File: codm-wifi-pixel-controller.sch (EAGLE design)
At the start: 45 parts, among them U1 AP62XXX-TSOT26, U2 REG710NA-5/250, U3 SN74AHCT125D, U4 ESP-WROOM-32

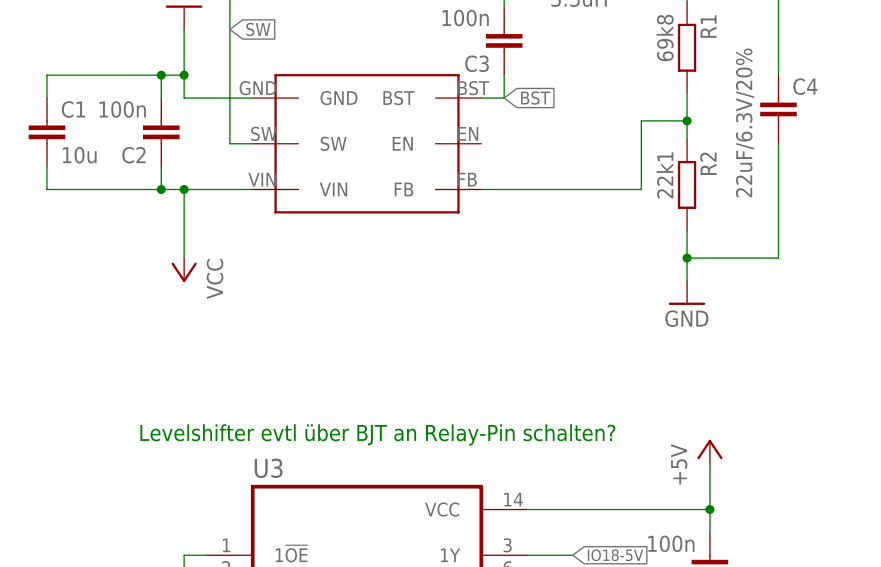
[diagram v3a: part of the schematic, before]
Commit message: added reverse polarity protection
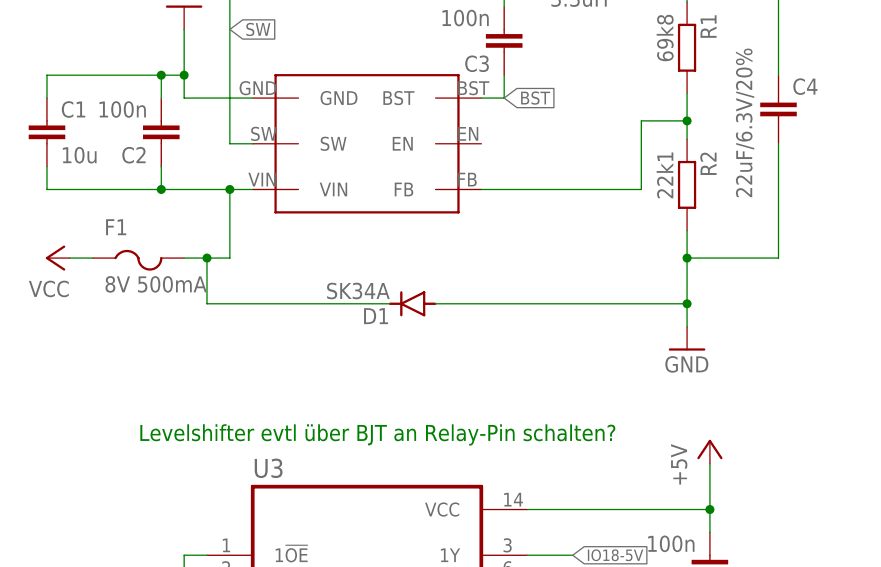
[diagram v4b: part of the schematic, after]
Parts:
- added D1: SK34A, diode:DIODE-DO214AC
- added F1: 8V 500mA, adafruit:PTCFUSE-1206
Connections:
- new net VCCF: C1.2, C2.1, D1.C, F1.2, U1.VIN
- net GND: now also D1.A
- net VCC: now also F1.1; no longer C1.2, C2.1, U1.VIN
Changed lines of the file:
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@@
 <part name="TP14" library="testpad" library_urn="urn:adsk.eagle:library:385" deviceset="PTR1" device="TP14R" package3d_urn="urn:adsk.eagle:package:27966/1" override_package3d_urn="urn:adsk.eagle:package:33701212/2" override_package_urn="urn:adsk.eagle:footprint:27923/1" value="PTR1TP14R"/>
 <part name="TP15" library="testpad" library_urn="urn:adsk.eagle:library:385" deviceset="PTR1" device="TP14R" package3d_urn="urn:adsk.eagle:package:27966/1" value="PTR1TP14R"/>
+<part name="D1" library="diode" deviceset="DIODE-" device="DO214AC" package3d_urn="urn:adsk.eagle:package:43417/2" value="SK34A"/>
+<part name="F1" library="adafruit" library_urn="urn:adsk.eagle:library:420" deviceset="PTCFUSE" device="-1206" package3d_urn="urn:adsk.eagle:package:6240569/1" override_package3d_urn="urn:adsk.eagle:package:20945049/2" override_package_urn="urn:adsk.eagle:footprint:6239923/1" value="8V 500mA"/>
 </parts>
 <sheets>
@@
 </instance>
 <instance part="U1" gate="G$1" x="45.72" y="139.7" smashed="yes"/>
-<instance part="P+3" gate="VCC" x="25.4" y="124.46" smashed="yes" rot="R180">
-<attribute name="VALUE" x="27.94" y="127" size="1.778" layer="96" rot="R270"/>
+<instance part="P+3" gate="VCC" x="10.16" y="127" smashed="yes" rot="R90">
+<attribute name="VALUE" x="12.7" y="124.46" size="1.778" layer="96" rot="R180"/>
 </instance>
 <instance part="GND5" gate="1" x="25.4" y="154.94" smashed="yes" rot="R180">
@@
 <attribute name="VALUE" x="77.978" y="138.938" size="1.778" layer="96" rot="R270"/>
 </instance>
-<instance part="GND3" gate="1" x="81.28" y="121.92" smashed="yes">
-<attribute name="VALUE" x="78.74" y="119.38" size="1.778" layer="96"/>
+<instance part="GND3" gate="1" x="81.28" y="116.84" smashed="yes">
+<attribute name="VALUE" x="78.74" y="114.3" size="1.778" layer="96"/>
 </instance>
 <instance part="C4" gate="G$1" x="91.44" y="144.78" smashed="yes">
@@
 <attribute name="NAME" x="92.964" y="41.91" size="1.778" layer="95" rot="R90"/>
 <attribute name="TP_SIGNAL_NAME" x="95.25" y="45.72" size="1.778" layer="97"/>
+</instance>
+<instance part="D1" gate="G$1" x="50.8" y="121.92" smashed="yes" rot="R180">
+<attribute name="NAME" x="48.26" y="121.4374" size="1.778" layer="95" rot="R180"/>
+<attribute name="VALUE" x="48.26" y="124.2314" size="1.778" layer="96" rot="R180"/>
+</instance>
+<instance part="F1" gate="G$1" x="20.32" y="124.46" smashed="yes">
+<attribute name="VALUE" x="16.51" y="123.19" size="1.778" layer="96"/>
+<attribute name="NAME" x="16.51" y="129.54" size="1.778" layer="95"/>
 </instance>
 </instances>
@@
 <pinref part="GND3" gate="1" pin="GND"/>
 <pinref part="C4" gate="G$1" pin="2"/>
-<wire x1="81.28" y1="127" x2="81.28" y2="124.46" width="0.1524" layer="91"/>
+<wire x1="81.28" y1="127" x2="81.28" y2="121.92" width="0.1524" layer="91"/>
+<wire x1="81.28" y1="121.92" x2="81.28" y2="119.38" width="0.1524" layer="91"/>
 <wire x1="91.44" y1="139.7" x2="91.44" y2="127" width="0.1524" layer="91"/>
 <wire x1="81.28" y1="127" x2="91.44" y2="127" width="0.1524" layer="91"/>
 <junction x="81.28" y="127"/>
+<pinref part="D1" gate="G$1" pin="A"/>
+<wire x1="81.28" y1="121.92" x2="53.34" y2="121.92" width="0.1524" layer="91"/>
+<junction x="81.28" y="121.92"/>
 </segment>
 <segment>
@@
 </segment>
 <segment>
+<pinref part="F1" gate="G$1" pin="1"/>
+<wire x1="15.24" y1="127" x2="12.7" y2="127" width="0.1524" layer="91"/>
 <pinref part="P+3" gate="VCC" pin="VCC"/>
-<wire x1="25.4" y1="127" x2="25.4" y2="134.62" width="0.1524" layer="91"/>
-<pinref part="U1" gate="G$1" pin="VIN"/>
-<wire x1="25.4" y1="134.62" x2="33.02" y2="134.62" width="0.1524" layer="91"/>
-<wire x1="25.4" y1="134.62" x2="22.86" y2="134.62" width="0.1524" layer="91"/>
-<junction x="25.4" y="134.62"/>
-<pinref part="C1" gate="G$1" pin="2"/>
-<wire x1="22.86" y1="134.62" x2="10.16" y2="134.62" width="0.1524" layer="91"/>
-<wire x1="10.16" y1="134.62" x2="10.16" y2="137.16" width="0.1524" layer="91"/>
-<pinref part="C2" gate="G$1" pin="1"/>
-<wire x1="22.86" y1="137.16" x2="22.86" y2="134.62" width="0.1524" layer="91"/>
-<junction x="22.86" y="134.62"/>
 </segment>
 </net>
@@
 </segment>
 </net>
+<net name="VCCF" class="0">
+<segment>
+<pinref part="D1" gate="G$1" pin="C"/>
+<wire x1="27.94" y1="127" x2="30.48" y2="127" width="0.1524" layer="91"/>
+<wire x1="48.26" y1="121.92" x2="27.94" y2="121.92" width="0.1524" layer="91"/>
+<wire x1="27.94" y1="121.92" x2="27.94" y2="127" width="0.1524" layer="91"/>
+<junction x="27.94" y="127"/>
+<pinref part="F1" gate="G$1" pin="2"/>
+<wire x1="25.4" y1="127" x2="27.94" y2="127" width="0.1524" layer="91"/>
+<wire x1="22.86" y1="134.62" x2="30.48" y2="134.62" width="0.1524" layer="91"/>
+<pinref part="C1" gate="G$1" pin="2"/>
+<wire x1="22.86" y1="134.62" x2="10.16" y2="134.62" width="0.1524" layer="91"/>
+<wire x1="10.16" y1="134.62" x2="10.16" y2="137.16" width="0.1524" layer="91"/>
+<pinref part="C2" gate="G$1" pin="1"/>
+<wire x1="22.86" y1="137.16" x2="22.86" y2="134.62" width="0.1524" layer="91"/>
+<junction x="22.86" y="134.62"/>
+<wire x1="30.48" y1="127" x2="30.48" y2="134.62" width="0.1524" layer="91"/>
+<pinref part="U1" gate="G$1" pin="VIN"/>
+<wire x1="33.02" y1="134.62" x2="30.48" y2="134.62" width="0.1524" layer="91"/>
+<junction x="30.48" y="134.62"/>
+</segment>
+</net>

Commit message: new version 0.7.4 with fixes
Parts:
- removed C8: 100n, rcl:C-EUC0603K
- added TP16: PTR1TP14R, testpad:PTR1TP14R
- JP1: device pinhead:PINHD-1X5 -> codm:PINHD-1X5
- U3: value SN74AHCT125D -> SN74AHCT125PWR; device SN74AHCT125D:SN74AHCT125D -> SN74AHCT125PWR:SN74AHCT125PWR
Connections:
- net BTN: now also S1.1; no longer S1.2
- net GND: now also FLASH.4, RESET.3, S1.2, TP16.TP, U3.!1OE, U3.!2OE, U3.!3OE, U3.!4OE; no longer C8.1, FLASH.2, RESET.1, S1.1, U3.1!OE, U3.2!OE, U3.3!OE, U3.4!OE
- net RESET: no longer C8.2
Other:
- note added: "WLAN Pixel Controller V0.7.4 codm.de, 2022 CC-BY-NC-SA"
- note removed: "WLAN Pixel Controller V0.7 codm.de, 2022 CC-BY-NC-SA"

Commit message: finetuning 0.7.4
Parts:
- removed R5: 10k, rcl:R-EU_R0603
- F1: value 8V 500mA -> 24V 500mA
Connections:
- net +3V3: no longer R5.1
- net GPIO0: no longer R5.2
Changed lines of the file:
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@@
 <part name="R4" library="rcl" deviceset="R-EU_" device="R0603" package3d_urn="urn:adsk.eagle:package:23555/3" value="10k"/>
 <part name="C5" library="rcl" deviceset="C-EU" device="C0603K" package3d_urn="urn:adsk.eagle:package:23680/2" value="1u"/>
-<part name="R5" library="rcl" deviceset="R-EU_" device="R0603" package3d_urn="urn:adsk.eagle:package:23555/3" value="10k"/>
-<part name="+3V3" library="supply1" deviceset="+3V3" device=""/>
 <part name="GND4" library="supply1" deviceset="GND" device=""/>
 <part name="U1" library="codm" library_urn="urn:adsk.eagle:library:11602856" deviceset="AP62XXX-TSOT26" device="" package3d_urn="urn:adsk.eagle:package:33659716/2"/>
@@
 <part name="TP15" library="testpad" library_urn="urn:adsk.eagle:library:385" deviceset="PTR1" device="TP14R" package3d_urn="urn:adsk.eagle:package:27966/1" value="PTR1TP14R"/>
 <part name="D1" library="diode" deviceset="DIODE-" device="DO214AC" package3d_urn="urn:adsk.eagle:package:43417/2" value="SK34A"/>
-<part name="F1" library="adafruit" library_urn="urn:adsk.eagle:library:420" deviceset="PTCFUSE" device="-1206" package3d_urn="urn:adsk.eagle:package:6240569/1" override_package3d_urn="urn:adsk.eagle:package:20945049/2" override_package_urn="urn:adsk.eagle:footprint:6239923/1" value="8V 500mA"/>
+<part name="F1" library="adafruit" library_urn="urn:adsk.eagle:library:420" deviceset="PTCFUSE" device="-1206" package3d_urn="urn:adsk.eagle:package:6240569/1" override_package3d_urn="urn:adsk.eagle:package:20945049/2" override_package_urn="urn:adsk.eagle:footprint:6239923/1" value="24V 500mA"/>
 <part name="TP16" library="testpad" library_urn="urn:adsk.eagle:library:385" deviceset="PTR1" device="TP14R" package3d_urn="urn:adsk.eagle:package:27966/1" value="PTR1TP14R"/>
 </parts>
@@
 <attribute name="NAME" x="153.416" y="83.439" size="1.778" layer="95" rot="R180"/>
 <attribute name="VALUE" x="153.416" y="88.519" size="1.778" layer="96" rot="R180"/>
-</instance>
-<instance part="R5" gate="G$1" x="231.14" y="89.408" smashed="yes" rot="R270">
-<attribute name="NAME" x="232.6386" y="93.218" size="1.778" layer="95" rot="R270"/>
-<attribute name="VALUE" x="227.838" y="93.218" size="1.778" layer="96" rot="R270"/>
-</instance>
-<instance part="+3V3" gate="G$1" x="231.14" y="111.76" smashed="yes">
-<attribute name="VALUE" x="228.6" y="106.68" size="1.778" layer="96" rot="R90"/>
 </instance>
 <instance part="GND4" gate="1" x="66.04" y="10.16" smashed="yes">
@@
 </segment>
 <segment>
-<pinref part="+3V3" gate="G$1" pin="+3V3"/>
-<pinref part="R5" gate="G$1" pin="1"/>
-<wire x1="231.14" y1="109.22" x2="231.14" y2="94.488" width="0.1524" layer="91"/>
-</segment>
-<segment>
 <pinref part="L1" gate="G$1" pin="2"/>
 <wire x1="78.74" y1="157.48" x2="81.28" y2="157.48" width="0.1524" layer="91"/>
@@
 <segment>
 <pinref part="U4" gate="G$1" pin="IO0"/>
-<wire x1="231.14" y1="50.8" x2="223.52" y2="50.8" width="0.1524" layer="91"/>
-<pinref part="R5" gate="G$1" pin="2"/>
-<wire x1="231.14" y1="84.328" x2="231.14" y2="50.8" width="0.1524" layer="91"/>
+<wire x1="233.68" y1="50.8" x2="223.52" y2="50.8" width="0.1524" layer="91"/>
 <pinref part="FLASH" gate="G$1" pin="1"/>
-<wire x1="231.14" y1="50.8" x2="233.68" y2="50.8" width="0.1524" layer="91"/>
-<junction x="231.14" y="50.8"/>
 </segment>
 </net>
@@
 <segment>
 <pinref part="D1" gate="G$1" pin="C"/>
-<wire x1="27.94" y1="127" x2="30.48" y2="127" width="0.1524" layer="91"/>
-<wire x1="48.26" y1="121.92" x2="27.94" y2="121.92" width="0.1524" layer="91"/>
-<wire x1="27.94" y1="121.92" x2="27.94" y2="127" width="0.1524" layer="91"/>
-<junction x="27.94" y="127"/>
+<wire x1="48.26" y1="121.92" x2="30.48" y2="121.92" width="0.1524" layer="91"/>
+<wire x1="30.48" y1="121.92" x2="30.48" y2="127" width="0.1524" layer="91"/>
+<junction x="30.48" y="127"/>
 <pinref part="F1" gate="G$1" pin="2"/>
-<wire x1="25.4" y1="127" x2="27.94" y2="127" width="0.1524" layer="91"/>
+<wire x1="25.4" y1="127" x2="30.48" y2="127" width="0.1524" layer="91"/>
 <wire x1="22.86" y1="134.62" x2="30.48" y2="134.62" width="0.1524" layer="91"/>
 <pinref part="C1" gate="G$1" pin="2"/>

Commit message: after prototype 0.7.4 - final 0.8
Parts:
- removed C12: 100n, rcl:C-EUC0603K
- added C8: 2.2uF, rcl:C-EUC0603K
- C11: value 2.2uF -> 100n
- renumbered R6 to R5
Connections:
- net +3V3: now also C9.2; no longer C10.2
- net +5V: now also C10.2; no longer C12.2
- net GND: now also C9.1; no longer C12.1
- net N$5: now also C8.1; no longer C9.1
- net N$8: now also C8.2; no longer C9.2
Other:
- moved on the sheet: C10, C11, C9
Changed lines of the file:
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@@
 <part name="U3" library="SN74AHCT125PWR" deviceset="SN74AHCT125PWR" device="" override_package3d_urn="urn:adsk.eagle:package:23111573/4" override_package_urn="urn:adsk.eagle:footprint:23111574/2" override_locally_modified="yes"/>
 <part name="GND2" library="supply1" deviceset="GND" device=""/>
-<part name="C12" library="rcl" deviceset="C-EU" device="C0603K" package3d_urn="urn:adsk.eagle:package:23680/2" value="100n"/>
+<part name="C11" library="rcl" deviceset="C-EU" device="C0603K" package3d_urn="urn:adsk.eagle:package:23680/2" value="100n"/>
 <part name="GND6" library="supply1" deviceset="GND" device=""/>
 <part name="P+2" library="supply1" library_urn="urn:adsk.eagle:library:371" deviceset="+5V" device=""/>
@@
 <part name="C2" library="rcl" deviceset="C-EU" device="C0603K" package3d_urn="urn:adsk.eagle:package:23680/2" value="100n"/>
 <part name="U2" library="REG710NA-5_250" deviceset="REG710NA-5/250" device="" override_package3d_urn="urn:adsk.eagle:package:30503030/3" override_package_urn="urn:adsk.eagle:footprint:30503033/1" override_locally_modified="yes"/>
+<part name="C9" library="rcl" deviceset="C-EU" device="C0603K" package3d_urn="urn:adsk.eagle:package:23680/2" value="2.2uF"/>
 <part name="C10" library="rcl" deviceset="C-EU" device="C0603K" package3d_urn="urn:adsk.eagle:package:23680/2" value="2.2uF"/>
-<part name="C11" library="rcl" deviceset="C-EU" device="C0603K" package3d_urn="urn:adsk.eagle:package:23680/2" value="2.2uF"/>
-<part name="C9" library="rcl" deviceset="C-EU" device="C0603K" package3d_urn="urn:adsk.eagle:package:23680/2" value="2.2uF"/>
+<part name="C8" library="rcl" deviceset="C-EU" device="C0603K" package3d_urn="urn:adsk.eagle:package:23680/2" value="2.2uF"/>
 <part name="GND8" library="supply1" deviceset="GND" device=""/>
 <part name="+3V2" library="supply1" deviceset="+3V3" device=""/>
@@
 <part name="S1" library="Eagle_WS-TASV (rev21c)" deviceset="430182070816" device="" package3d_urn="urn:adsk.eagle:package:18304298/2" value="430182070816"/>
 <part name="GND12" library="supply1" deviceset="GND" device=""/>
-<part name="R6" library="rcl" deviceset="R-EU_" device="R0603" package3d_urn="urn:adsk.eagle:package:23555/3" value="10k"/>
+<part name="R5" library="rcl" deviceset="R-EU_" device="R0603" package3d_urn="urn:adsk.eagle:package:23555/3" value="10k"/>
 <part name="+3V4" library="supply1" deviceset="+3V3" device=""/>
 <part name="TP10" library="testpad" library_urn="urn:adsk.eagle:library:385" deviceset="PTR1" device="TP14R" package3d_urn="urn:adsk.eagle:package:27966/1" override_package3d_urn="urn:adsk.eagle:package:33701210/2" override_package_urn="urn:adsk.eagle:footprint:27923/1" value="PTR1TP14R"/>
@@
 <attribute name="VALUE" x="22.86" y="55.88" size="1.778" layer="96"/>
 </instance>
-<instance part="C12" gate="G$1" x="83.82" y="91.44" smashed="yes" rot="R180">
+<instance part="C11" gate="G$1" x="83.82" y="91.44" smashed="yes" rot="R180">
 <attribute name="NAME" x="82.296" y="91.059" size="1.778" layer="95" rot="R180"/>
 <attribute name="VALUE" x="82.296" y="96.139" size="1.778" layer="96" rot="R180"/>
@@
 <attribute name="VALUE" x="170.18" y="135.7" size="2.0828" layer="96" ratio="10" rot="SR0"/>
 </instance>
-<instance part="C10" gate="G$1" x="157.48" y="142.24" smashed="yes" rot="R180">
+<instance part="C9" gate="G$1" x="157.48" y="142.24" smashed="yes" rot="R180">
 <attribute name="NAME" x="155.956" y="141.859" size="1.778" layer="95" rot="R180"/>
 <attribute name="VALUE" x="155.956" y="146.939" size="1.778" layer="96" rot="R180"/>
 </instance>
-<instance part="C11" gate="G$1" x="208.28" y="149.86" smashed="yes" rot="R180">
+<instance part="C10" gate="G$1" x="208.28" y="149.86" smashed="yes" rot="R180">
 <attribute name="NAME" x="206.756" y="149.479" size="1.778" layer="95" rot="R180"/>
 <attribute name="VALUE" x="206.756" y="154.559" size="1.778" layer="96" rot="R180"/>
 </instance>
-<instance part="C9" gate="G$1" x="157.48" y="157.48" smashed="yes" rot="R270">
+<instance part="C8" gate="G$1" x="157.48" y="157.48" smashed="yes" rot="R270">
 <attribute name="NAME" x="157.861" y="155.956" size="1.778" layer="95" rot="R270"/>
 <attribute name="VALUE" x="152.781" y="155.956" size="1.778" layer="96" rot="R270"/>
@@
 <attribute name="VALUE" x="121.92" y="111.76" size="1.778" layer="96"/>
 </instance>
-<instance part="R6" gate="G$1" x="121.92" y="137.668" smashed="yes" rot="R270">
+<instance part="R5" gate="G$1" x="121.92" y="137.668" smashed="yes" rot="R270">
 <attribute name="NAME" x="123.4186" y="141.478" size="1.778" layer="95" rot="R270"/>
 <attribute name="VALUE" x="118.618" y="141.478" size="1.778" layer="96" rot="R270"/>
@@
 </segment>
 <segment>
-<pinref part="C12" gate="G$1" pin="1"/>
+<pinref part="C11" gate="G$1" pin="1"/>
 <wire x1="83.82" y1="88.9" x2="83.82" y2="68.58" width="0.1524" layer="91"/>
 <pinref part="GND6" gate="1" pin="GND"/>
@@
 <wire x1="208.28" y1="142.24" x2="208.28" y2="137.16" width="0.1524" layer="91"/>
 <pinref part="GND8" gate="1" pin="GND"/>
-<pinref part="C10" gate="G$1" pin="1"/>
+<pinref part="C9" gate="G$1" pin="1"/>
 <wire x1="208.28" y1="137.16" x2="208.28" y2="134.62" width="0.1524" layer="91"/>
 <wire x1="157.48" y1="139.7" x2="157.48" y2="137.16" width="0.1524" layer="91"/>
 <wire x1="157.48" y1="137.16" x2="208.28" y2="137.16" width="0.1524" layer="91"/>
 <junction x="208.28" y="137.16"/>
-<pinref part="C11" gate="G$1" pin="1"/>
+<pinref part="C10" gate="G$1" pin="1"/>
 <wire x1="208.28" y1="147.32" x2="208.28" y2="142.24" width="0.1524" layer="91"/>
 <junction x="208.28" y="142.24"/>
@@
 <pinref part="U3" gate="A" pin="VCC"/>
 <wire x1="63.5" y1="99.06" x2="83.82" y2="99.06" width="0.1524" layer="91"/>
-<pinref part="C12" gate="G$1" pin="2"/>
+<pinref part="C11" gate="G$1" pin="2"/>
 <wire x1="83.82" y1="99.06" x2="83.82" y2="96.52" width="0.1524" layer="91"/>
 <wire x1="83.82" y1="99.06" x2="83.82" y2="104.14" width="0.1524" layer="91"/>
@@
 <wire x1="200.66" y1="157.48" x2="208.28" y2="157.48" width="0.1524" layer="91"/>
 <pinref part="P+4" gate="1" pin="+5V"/>
-<pinref part="C11" gate="G$1" pin="2"/>
+<pinref part="C10" gate="G$1" pin="2"/>
 <wire x1="208.28" y1="157.48" x2="215.9" y2="157.48" width="0.1524" layer="91"/>
 <wire x1="208.28" y1="154.94" x2="208.28" y2="157.48" width="0.1524" layer="91"/>
@@
 <pinref part="+3V2" gate="G$1" pin="+3V3"/>
 <wire x1="144.78" y1="152.4" x2="157.48" y2="152.4" width="0.1524" layer="91"/>
-<pinref part="C10" gate="G$1" pin="2"/>
+<pinref part="C9" gate="G$1" pin="2"/>
 <wire x1="157.48" y1="152.4" x2="165.1" y2="152.4" width="0.1524" layer="91"/>
 <wire x1="157.48" y1="147.32" x2="157.48" y2="149.86" width="0.1524" layer="91"/>
@@
 <segment>
 <pinref part="+3V4" gate="G$1" pin="+3V3"/>
-<pinref part="R6" gate="G$1" pin="1"/>
+<pinref part="R5" gate="G$1" pin="1"/>
 <wire x1="121.92" y1="147.32" x2="121.92" y2="142.748" width="0.1524" layer="91"/>
 </segment>
@@
 <segment>
 <pinref part="U2" gate="A" pin="CPUMP+"/>
-<pinref part="C9" gate="G$1" pin="1"/>
+<pinref part="C8" gate="G$1" pin="1"/>
 <wire x1="165.1" y1="157.48" x2="160.02" y2="157.48" width="0.1524" layer="91"/>
 </segment>
@@
 <net name="N$8" class="0">
 <segment>
-<pinref part="C9" gate="G$1" pin="2"/>
+<pinref part="C8" gate="G$1" pin="2"/>
 <wire x1="152.4" y1="157.48" x2="149.86" y2="157.48" width="0.1524" layer="91"/>
 <wire x1="149.86" y1="157.48" x2="149.86" y2="154.94" width="0.1524" layer="91"/>
@@
 <net name="BTN" class="0">
 <segment>
-<pinref part="R6" gate="G$1" pin="2"/>
+<pinref part="R5" gate="G$1" pin="2"/>
 <wire x1="121.92" y1="129.54" x2="116.84" y2="129.54" width="0.1524" layer="91"/>
 <wire x1="121.92" y1="132.588" x2="121.92" y2="129.54" width="0.1524" layer="91"/>

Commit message: final V0.8, edited readme
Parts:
- LED: value 150080RS75000 -> 150080GS75000
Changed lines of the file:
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@@
 <part name="+3V31" library="supply1" deviceset="+3V3" device=""/>
 <part name="R3" library="rcl" deviceset="R-EU_" device="R0603" package3d_urn="urn:adsk.eagle:package:23555/3" value="2k7"/>
-<part name="LED" library="led" library_urn="urn:adsk.eagle:library:259" deviceset="LED" device="CHIP-LED0805" package3d_urn="urn:adsk.eagle:package:15818/2" value="150080RS75000"/>
+<part name="LED" library="led" library_urn="urn:adsk.eagle:library:259" deviceset="LED" device="CHIP-LED0805" package3d_urn="urn:adsk.eagle:package:15818/2" override_package3d_urn="urn:adsk.eagle:package:34599476/2" override_package_urn="urn:adsk.eagle:footprint:15672/1" value="150080GS75000"/>
 <part name="C6" library="rcl" deviceset="C-EU" device="C0603K" package3d_urn="urn:adsk.eagle:package:23680/2" value="100n"/>
 <part name="R4" library="rcl" deviceset="R-EU_" device="R0603" package3d_urn="urn:adsk.eagle:package:23555/3" value="10k"/>
